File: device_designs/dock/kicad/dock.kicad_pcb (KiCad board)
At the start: 5 copper layers, 160 x 100 mm, 9 parts, among them J1 USBC_UP, J5 RJ45, J6 POGO, U1 JHL9040, U2 TPS65994, U3 RTL8156, U4 VL817, U5 TPS55288, U8 DWM3001C

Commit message: feat(eda): Cont VI KiCad 10.0.5 CLI validation + PCB load fixes
Install path resolved; run ERC/DRC/Gerber/drill/PnP/STEP for all five boards.
Fix KiCad 10 PCB load blockers (unknown setup key on Student/DS-XL; odd
5-layer copper on Dock → 4-layer). Record RING_KICAD_CLI_VALIDATION_PASS
and honest per-board violation counts; NDA release posture unchanged.

Co-authored-by: Cursor <cursoragent@cursor.com>
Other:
- copper layers 5 -> 4
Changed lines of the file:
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@@
     (company "gunnchOS3k")
     (comment 1 "DOCK DIGITAL PCB PACKAGE — NOT fab-ready")
-    (comment 2 "kicad-cli ABSENT → EDMUND_ACTION_REQUIRED for ERC/DRC")
+    (comment 2 "Cont VI: kicad-cli 10.0.5 validation; 4-layer copper (In3 removed — KiCad even-layer rule)")
     (comment 3 "PHYSICAL_EXECUTION_FREEZE ACTIVE — no fab, no purchase, draft digital only")
   )
   (layers
-    (0 "F.Cu" signal) (1 "In1.Cu" signal) (2 "In2.Cu" signal) (3 "In3.Cu" signal)
+    (0 "F.Cu" signal) (1 "In1.Cu" signal) (2 "In2.Cu" signal)
     (31 "B.Cu" signal) (37 "F.SilkS" user "F.Silkscreen") (39 "F.Mask" user) (44 "Edge.Cuts" user)
   )

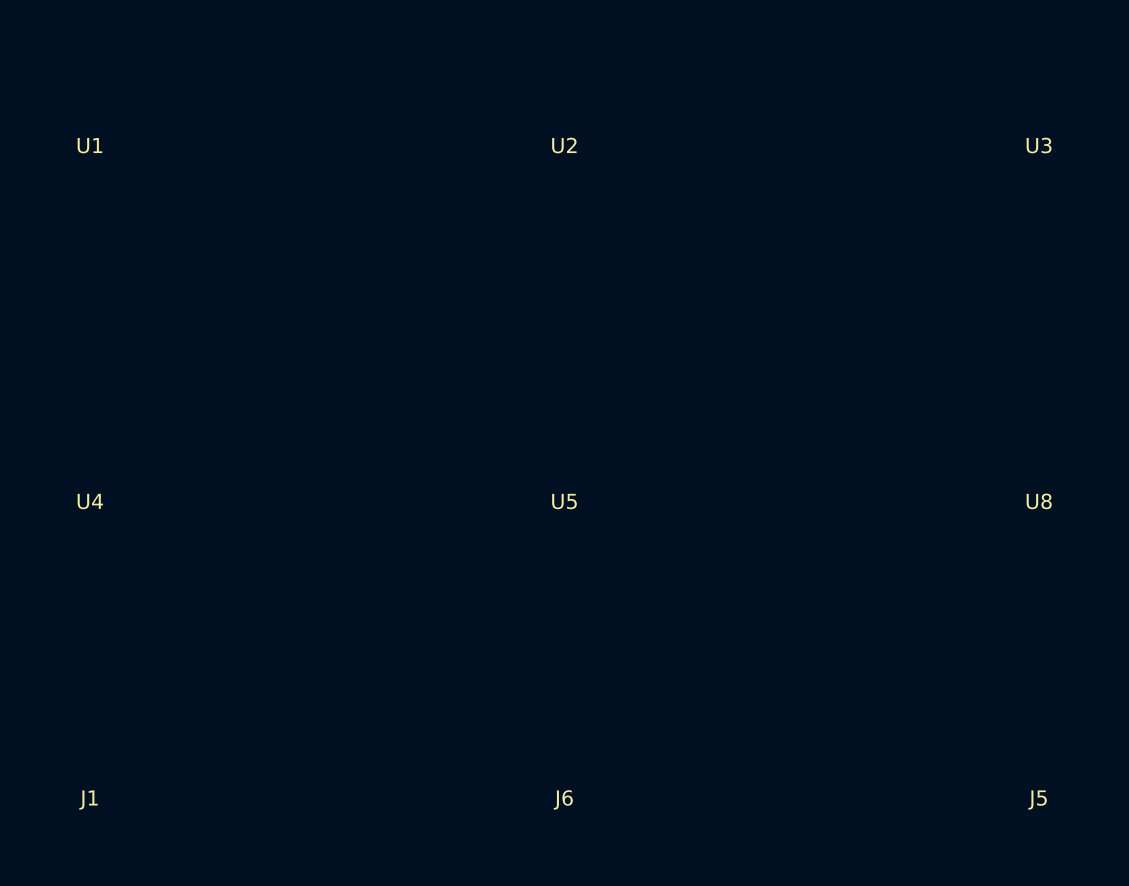
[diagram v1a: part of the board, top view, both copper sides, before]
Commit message: fix(dock): repair KiCad 10 PCB layer stack and export DRC/Gerber/STEP
Dock PCB used an invalid copper-layer/stackup combination that blocked
kicad-cli DRC; Cont VI now exports dock evidence and refreshes ERC/DRC
status without claiming ERC/DRC PASS or FULL release complete.

Co-authored-by: Cursor <cursoragent@cursor.com>
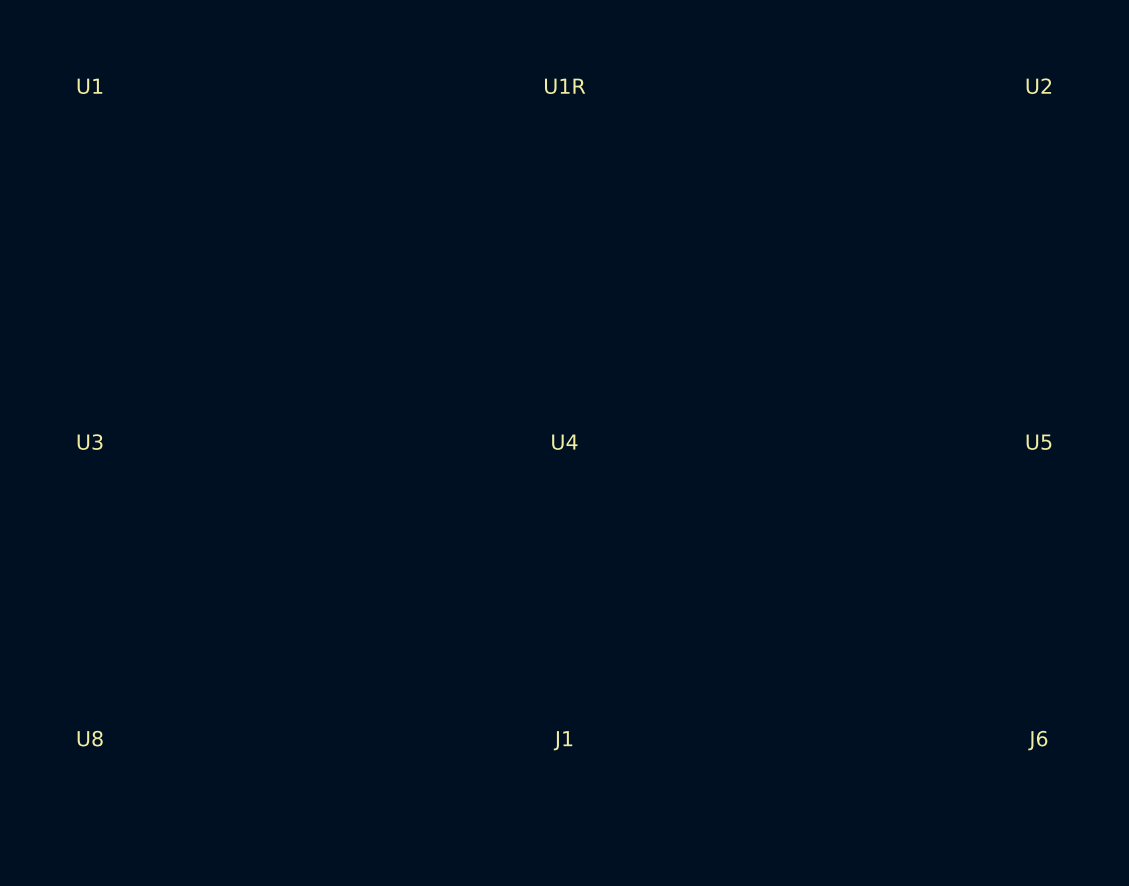
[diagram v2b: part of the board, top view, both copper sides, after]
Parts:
- removed J5: RJ45, Package_DFN_QFN:QFN-48-1EP_7x7mm_P0.5mm
- added U1R: JHL9040R, Package_DFN_QFN:QFN-48-1EP_7x7mm_P0.5mm, F.Cu at (70.0, 25.0)
- U1: value JHL9040 -> JHL8440
- U2: value TPS65994 -> TPS65994ADFBRQ1
- U5: value TPS55288 -> TPS55288RPMR
- moved U3 83.8 mm to (30.0, 55.0)
- moved U8 82.5 mm to (30.0, 80.0)
- moved J1 40.3 mm to (70.0, 80.0)
- moved J6 40.3 mm to (110.0, 80.0)
- moved U2 40.3 mm to (110.0, 25.0)
- moved U4 40.3 mm to (70.0, 55.0)
- moved U5 40.3 mm to (110.0, 55.0)
- moved U1 5.00 mm to (30.0, 25.0)
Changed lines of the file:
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@@
-(kicad_pcb (version 20221018) (generator "family_depth_digital")
+(kicad_pcb (version 20221018) (generator "continuation_vi_eda_closure")
   (general (thickness 1.6) (legacy_teardrops no))
   (paper "A4")
@@
     (title "dock_main_pcb")
     (date "2026-08-08")
-    (rev "0.2.0-dev")
+    (rev "0.3.0-cont-vi")
     (company "gunnchOS3k")
-    (comment 1 "DOCK DIGITAL PCB PACKAGE — NOT fab-ready")
-    (comment 2 "Cont VI: kicad-cli 10.0.5 validation; 4-layer copper (In3 removed — KiCad even-layer rule)")
+    (comment 1 "DOCK DIGITAL PCB PACKAGE — USB4/TB4 40G — NOT fab-ready")
+    (comment 2 "ADR-HW-002: JHL8440 controller + JHL9040R retimer; TB5 rejected")
     (comment 3 "PHYSICAL_EXECUTION_FREEZE ACTIVE — no fab, no purchase, draft digital only")
   )
   (layers
-    (0 "F.Cu" signal) (1 "In1.Cu" signal) (2 "In2.Cu" signal)
-    (31 "B.Cu" signal) (37 "F.SilkS" user "F.Silkscreen") (39 "F.Mask" user) (44 "Edge.Cuts" user)
+    (0 "F.Cu" signal) (1 "In1.Cu" signal) (2 "In2.Cu" signal) (31 "B.Cu" signal)
+    (37 "F.SilkS" user "F.Silkscreen") (39 "F.Mask" user) (44 "Edge.Cuts" user)
   )
-  (setup (pad_to_mask_clearance 0.051) (stackup
-    (layer "F.Cu" (type "copper") (thickness 0.035))
-    (layer "dielectric1" (type "core") (thickness 0.2) (material "FR4") (epsilon_r 4.5) (loss_tangent 0.02))
-    (layer "In1.Cu" (type "copper") (thickness 0.035))
-    (layer "dielectric2" (type "core") (thickness 0.7) (material "FR4") (epsilon_r 4.5) (loss_tangent 0.02))
-    (layer "In2.Cu" (type "copper") (thickness 0.035))
-    (layer "dielectric3" (type "core") (thickness 0.2) (material "FR4") (epsilon_r 4.5) (loss_tangent 0.02))
-    (layer "B.Cu" (type "copper") (thickness 0.035))
-  ))
+  (setup (pad_to_mask_clearance 0.051))
   (gr_rect (start 0 0) (end 160 100) (stroke (width 0.1) (type default)) (fill none) (layer "Edge.Cuts"))
   (footprint "Package_DFN_QFN:QFN-48-1EP_7x7mm_P0.5mm" (layer "F.Cu")
-    (at 30 30)
+    (at 30 25)
     (property "Reference" "U1" (at 0 -2.5 0) (layer "F.SilkS"))
-    (property "Value" "JHL9040" (at 0 2.5 0) (layer "F.Fab"))
+    (property "Value" "JHL8440" (at 0 2.5 0) (layer "F.Fab"))
     (attr smd)
   )
   (footprint "Package_DFN_QFN:QFN-48-1EP_7x7mm_P0.5mm" (layer "F.Cu")
-    (at 70 30)
-    (property "Reference" "U2" (at 0 -2.5 0) (layer "F.SilkS"))
-    (property "Value" "TPS65994" (at 0 2.5 0) (layer "F.Fab"))
+    (at 70 25)
+    (property "Reference" "U1R" (at 0 -2.5 0) (layer "F.SilkS"))
+    (property "Value" "JHL9040R" (at 0 2.5 0) (layer "F.Fab"))
     (attr smd)
   )
   (footprint "Package_DFN_QFN:QFN-48-1EP_7x7mm_P0.5mm" (layer "F.Cu")
-    (at 110 30)
+    (at 110 25)
+    (property "Reference" "U2" (at 0 -2.5 0) (layer "F.SilkS"))
+    (property "Value" "TPS65994ADFBRQ1" (at 0 2.5 0) (layer "F.Fab"))
+    (attr smd)
+  )
+  (footprint "Package_DFN_QFN:QFN-48-1EP_7x7mm_P0.5mm" (layer "F.Cu")
+    (at 30 55)
     (property "Reference" "U3" (at 0 -2.5 0) (layer "F.SilkS"))
     (property "Value" "RTL8156" (at 0 2.5 0) (layer "F.Fab"))
@@
   )
   (footprint "Package_DFN_QFN:QFN-48-1EP_7x7mm_P0.5mm" (layer "F.Cu")
-    (at 30 60)
+    (at 70 55)
     (property "Reference" "U4" (at 0 -2.5 0) (layer "F.SilkS"))
     (property "Value" "VL817" (at 0 2.5 0) (layer "F.Fab"))
@@
   )
   (footprint "Package_DFN_QFN:QFN-48-1EP_7x7mm_P0.5mm" (layer "F.Cu")
-    (at 70 60)
+    (at 110 55)
     (property "Reference" "U5" (at 0 -2.5 0) (layer "F.SilkS"))
-    (property "Value" "TPS55288" (at 0 2.5 0) (layer "F.Fab"))
+    (property "Value" "TPS55288RPMR" (at 0 2.5 0) (layer "F.Fab"))
     (attr smd)
   )
   (footprint "Package_DFN_QFN:QFN-48-1EP_7x7mm_P0.5mm" (layer "F.Cu")
-    (at 110 60)
+    (at 30 80)
     (property "Reference" "U8" (at 0 -2.5 0) (layer "F.SilkS"))
     (property "Value" "DWM3001C" (at 0 2.5 0) (layer "F.Fab"))
@@
   )
   (footprint "Package_DFN_QFN:QFN-48-1EP_7x7mm_P0.5mm" (layer "F.Cu")
-    (at 30 85)
+    (at 70 80)
     (property "Reference" "J1" (at 0 -2.5 0) (layer "F.SilkS"))
     (property "Value" "USBC_UP" (at 0 2.5 0) (layer "F.Fab"))
@@
   )
   (footprint "Package_DFN_QFN:QFN-48-1EP_7x7mm_P0.5mm" (layer "F.Cu")
-    (at 70 85)
+    (at 110 80)
     (property "Reference" "J6" (at 0 -2.5 0) (layer "F.SilkS"))
     (property "Value" "POGO" (at 0 2.5 0) (layer "F.Fab"))
     (attr smd)
   )
-  (footprint "Package_DFN_QFN:QFN-48-1EP_7x7mm_P0.5mm" (layer "F.Cu")
-    (at 110 85)
-    (property "Reference" "J5" (at 0 -2.5 0) (layer "F.SilkS"))
-    (property "Value" "RJ45" (at 0 2.5 0) (layer "F.Fab"))
-    (attr smd)
-  )

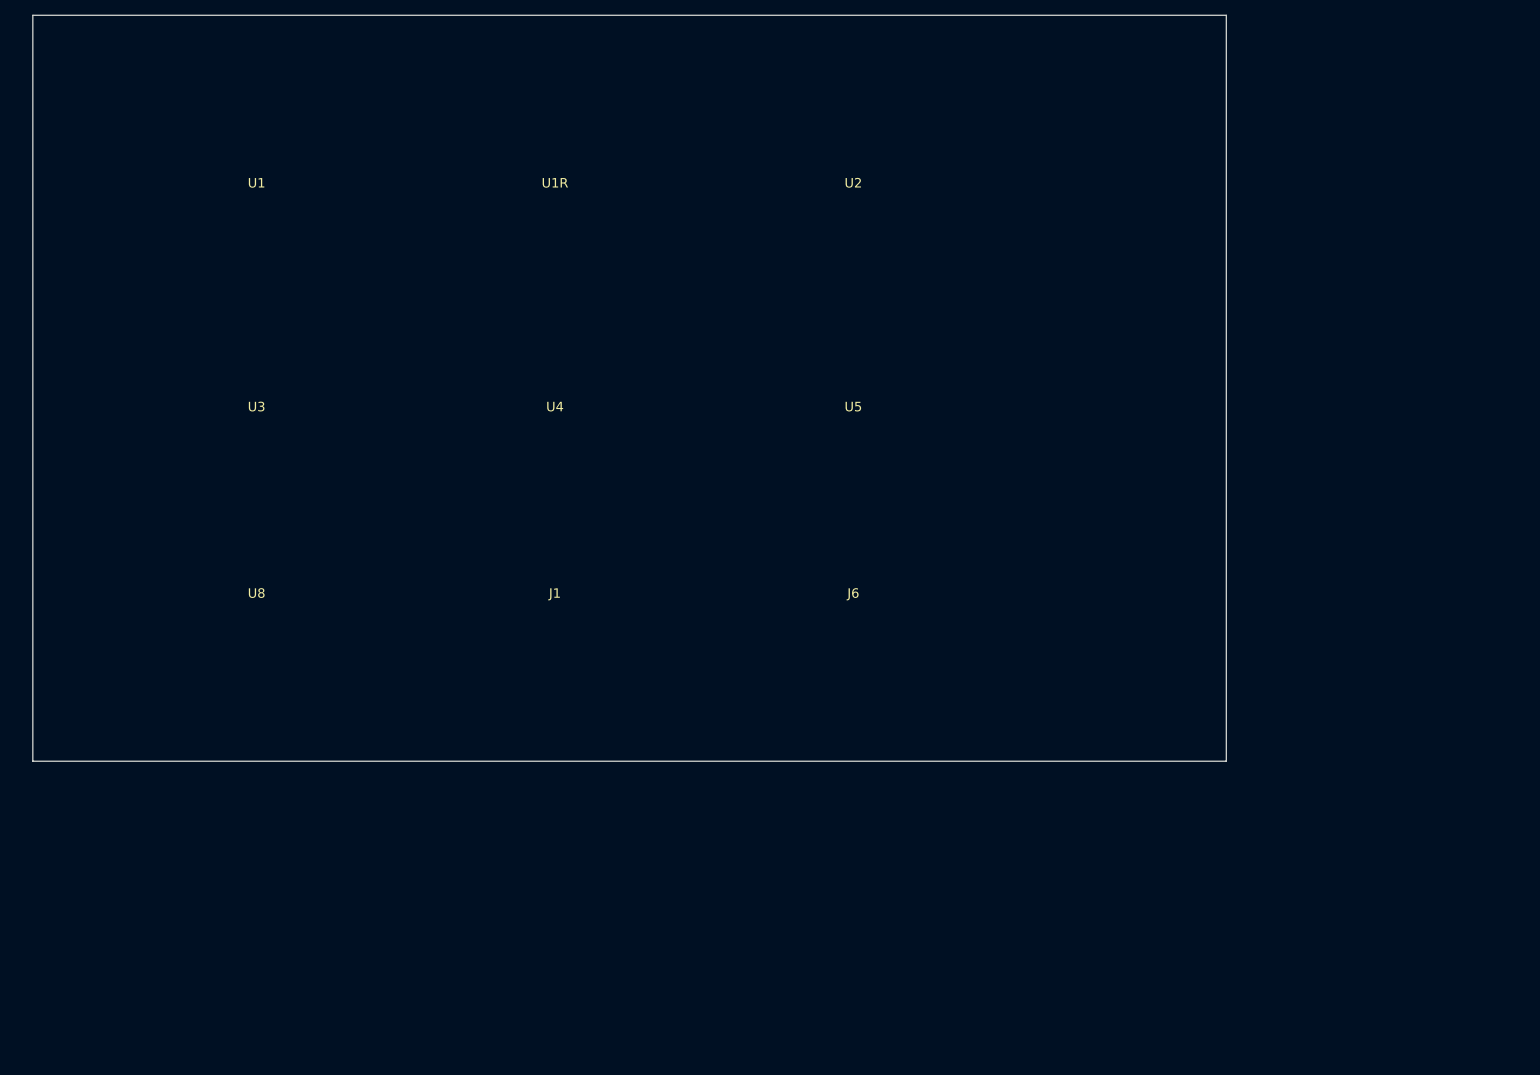
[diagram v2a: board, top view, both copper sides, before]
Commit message: feat(eda): Cont VII release-clean ledger + ERC/DRC zero-error revalidation
Investigate every Cont VI ERC/DRC entry, wire functional nets, clear error-class
violations, and publish honest release-clean tokens (CLI pass ≠ clean pass).

Co-authored-by: Cursor <cursoragent@cursor.com>
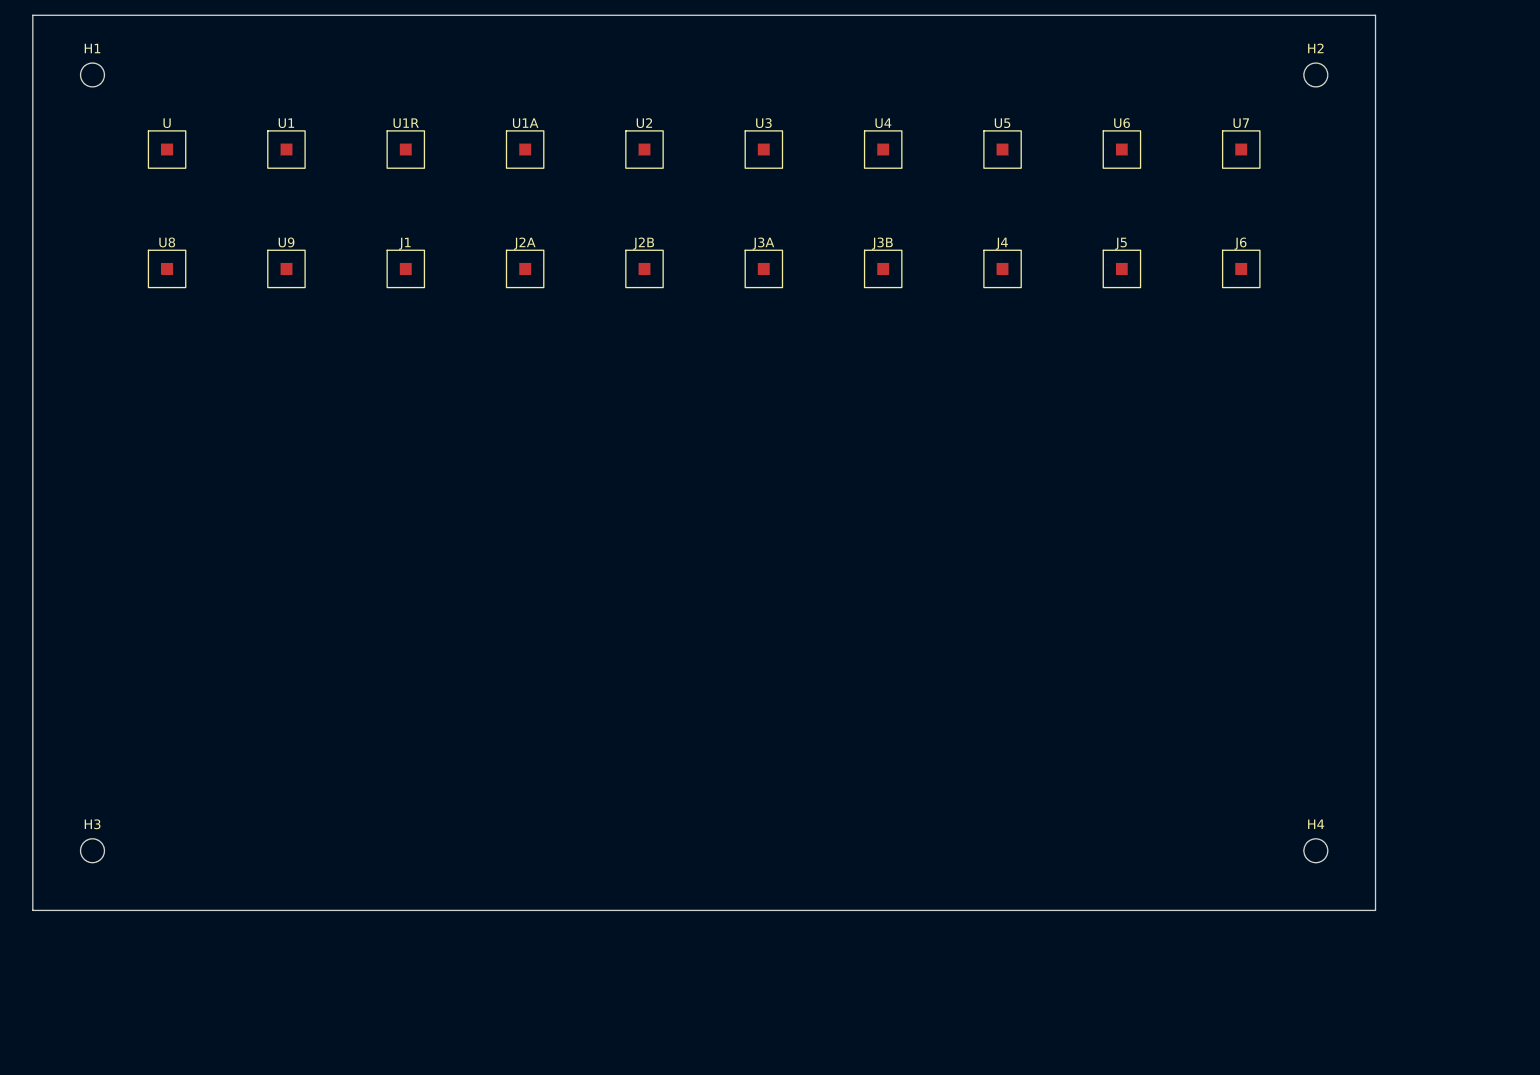
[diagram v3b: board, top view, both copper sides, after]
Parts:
- removed the U1R at (70.0, 25.0)
- added H1: M3, gunnchos_structural:MountingHole_3.2mm, F.Cu at (8.00, 8.00)
- added H2: M3, gunnchos_structural:MountingHole_3.2mm, F.Cu at (172.0, 8.00)
- added H3: M3, gunnchos_structural:MountingHole_3.2mm, F.Cu at (8.00, 112.0)
- added H4: M3, gunnchos_structural:MountingHole_3.2mm, F.Cu at (172.0, 112.0)
- added J2A: USB4085, gunnchos_structural:Block_SMD_10x10, F.Cu at (66.0, 34.0)
- added J2B: USB4085, gunnchos_structural:Block_SMD_10x10, F.Cu at (82.0, 34.0)
- added J3A: USB3_A, gunnchos_structural:Block_SMD_10x10, F.Cu at (98.0, 34.0)
- added J3B: USB3_A, gunnchos_structural:Block_SMD_10x10, F.Cu at (114.0, 34.0)
- added J4: HDMI_TypeA, gunnchos_structural:Block_SMD_10x10, F.Cu at (130.0, 34.0)
- added J5: JK0-0136NL, gunnchos_structural:Block_SMD_10x10, F.Cu at (146.0, 34.0)
- added U: FuncBlock, gunnchos_structural:Block_SMD_10x10, F.Cu at (18.0, 18.0)
- added U1A: VL108, gunnchos_structural:Block_SMD_10x10, F.Cu at (66.0, 18.0)
- added U1R: JHL9040R, gunnchos_structural:Block_SMD_10x10, F.Cu at (50.0, 18.0)
- added U6: TPS62864, gunnchos_structural:Block_SMD_10x10, F.Cu at (146.0, 18.0)
- added U7: TLV75533PDRVR, gunnchos_structural:Block_SMD_10x10, F.Cu at (162.0, 18.0)
- added U9: ALC4050, gunnchos_structural:Block_SMD_10x10, F.Cu at (34.0, 34.0)
- J1: value USBC_UP -> USB4085; footprint Package_DFN_QFN:QFN-48-1EP_7x7mm_P0.5mm -> gunnchos_structural:Block_SMD_10x10
- J6: value POGO -> Mill-Max_pogo; footprint Package_DFN_QFN:QFN-48-1EP_7x7mm_P0.5mm -> gunnchos_structural:Block_SMD_10x10
- U1, U2, U3, U4, U5, U8: footprint Package_DFN_QFN:QFN-48-1EP_7x7mm_P0.5mm -> gunnchos_structural:Block_SMD_10x10
- moved U3 77.4 mm to (98.0, 18.0)
- moved J6 69.4 mm to (162.0, 34.0)
- moved U4 57.5 mm to (114.0, 18.0)
- moved J1 50.2 mm to (50.0, 34.0)
- moved U8 47.5 mm to (18.0, 34.0)
- moved U5 42.1 mm to (130.0, 18.0)
- moved U2 28.9 mm to (82.0, 18.0)
- moved U1 8.06 mm to (34.0, 18.0)
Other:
- board size 160 x 100 mm -> 180 x 120 mm
- rule pad_to_mask_clearance: 0.051 -> 0.0
